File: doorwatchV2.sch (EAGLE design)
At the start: 44 parts, among them IC1 LM2576S-5.0, IC2 MAX3232CPE, K1 FINDER-43.61, Q1 IRLZ44Z, T1 BC847, T2 BC847, T3 BC847, T4 BC847, X1 MKDSN1,5/2-5,08, X2 D-SUB9-H2M09RA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

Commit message: updated the package of the inductor and updated the layout
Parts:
- L1: device rcl:L-EU0207/12 -> rcl:L-EU2200-20.32
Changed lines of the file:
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@@
 <part name="IC1" library="regulators" deviceset="LM2576" device="S" value="LM2576S-5.0"/>
 <part name="GND1" library="supply1" deviceset="GND" device=""/>
-<part name="L1" library="rcl" deviceset="L-EU" device="0207/12" value="100uH"/>
+<part name="L1" library="rcl" deviceset="L-EU" device="2200-20.32" value="100uH"/>
 <part name="D1" library="diode" deviceset="1N581*" device="" technology="7-B"/>
 <part name="C1" library="rcl" deviceset="CPOL-EU" device="E2.5-7" value="100uF"/>

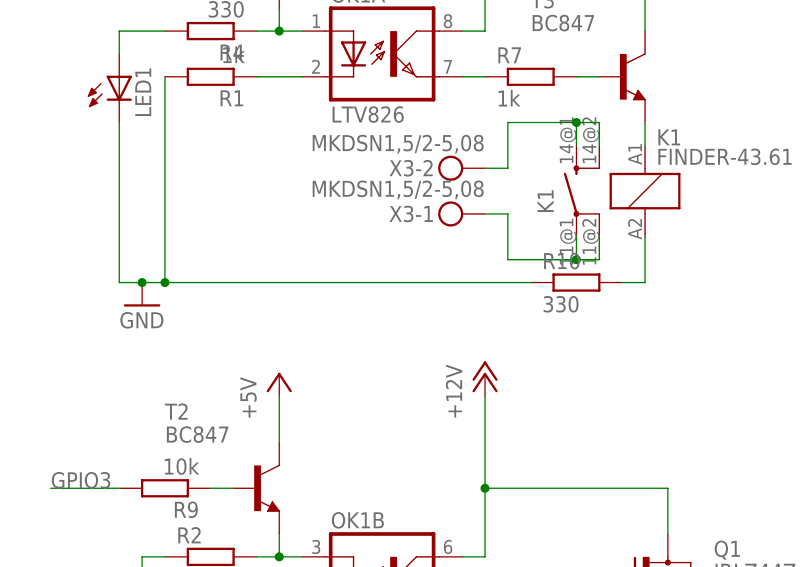
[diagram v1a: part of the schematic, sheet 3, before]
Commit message: removed resistor in relai circuit -> voltage was to low
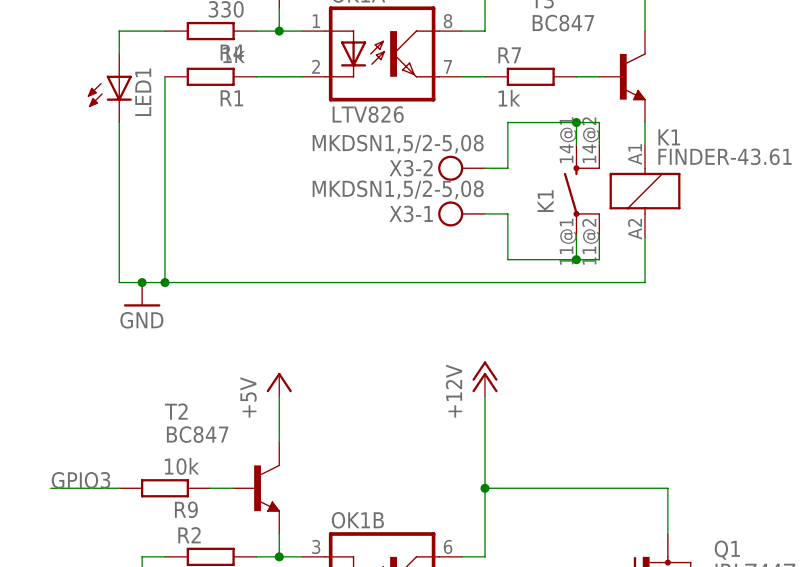
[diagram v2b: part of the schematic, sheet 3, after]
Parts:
- removed R10: 330, rcl:R-EU_M0805
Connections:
- removed net N$26: K1K.2, R10.2
- net GND: now also K1K.2; no longer R10.1
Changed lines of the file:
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@@
 <part name="R9" library="rcl" deviceset="R-EU_" device="M0805" value="10k"/>
 <part name="T3" library="transistor" deviceset="BC847" device=""/>
-<part name="R10" library="rcl" deviceset="R-EU_" device="M0805" value="330"/>
 <part name="LED4" library="led" deviceset="LED" device="CHIP-LED0805"/>
 <part name="R11" library="rcl" deviceset="R-EU_" device="M0805" value="330"/>
@@
 <instance part="R9" gate="G$1" x="-66.04" y="-43.18" rot="R180"/>
 <instance part="T3" gate="G$1" x="-15.24" y="2.54"/>
-<instance part="R10" gate="G$1" x="-20.32" y="-20.32"/>
 <instance part="LED4" gate="G$1" x="-66.04" y="-99.06" rot="R270"/>
 <instance part="R11" gate="G$1" x="-55.88" y="-99.06" rot="R180"/>
@@
 <wire x1="-68.58" y1="-20.32" x2="-66.04" y2="-20.32" width="0.1524" layer="91"/>
 <junction x="-68.58" y="-20.32"/>
-<pinref part="R10" gate="G$1" pin="1"/>
-<wire x1="-25.4" y1="-20.32" x2="-66.04" y2="-20.32" width="0.1524" layer="91"/>
+<wire x1="-12.7" y1="-20.32" x2="-66.04" y2="-20.32" width="0.1524" layer="91"/>
 <junction x="-66.04" y="-20.32"/>
+<pinref part="K1" gate="K" pin="2"/>
+<wire x1="-12.7" y1="-15.24" x2="-12.7" y2="-20.32" width="0.1524" layer="91"/>
 </segment>
 <segment>
@@
 </segment>
 </net>
-<net name="N$26" class="0">
-<segment>
-<pinref part="K1" gate="K" pin="2"/>
-<pinref part="R10" gate="G$1" pin="2"/>
-<wire x1="-12.7" y1="-15.24" x2="-12.7" y2="-20.32" width="0.1524" layer="91"/>
-<wire x1="-12.7" y1="-20.32" x2="-15.24" y2="-20.32" width="0.1524" layer="91"/>
-</segment>
-</net>
